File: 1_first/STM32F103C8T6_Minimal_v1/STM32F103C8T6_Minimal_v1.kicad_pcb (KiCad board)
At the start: 2 copper layers, 51.1 x 41.1 mm, 34 parts, among them J1 Conn_01x06, J2 USB_B_Micro, SW1 SW_SPDT, SW2 SW_Push, SW3 SW_Push, U1 AMS1117-3.3, U2 STM32F103C8Tx, U3 USBLC6-2SC6, Y1 8MHz

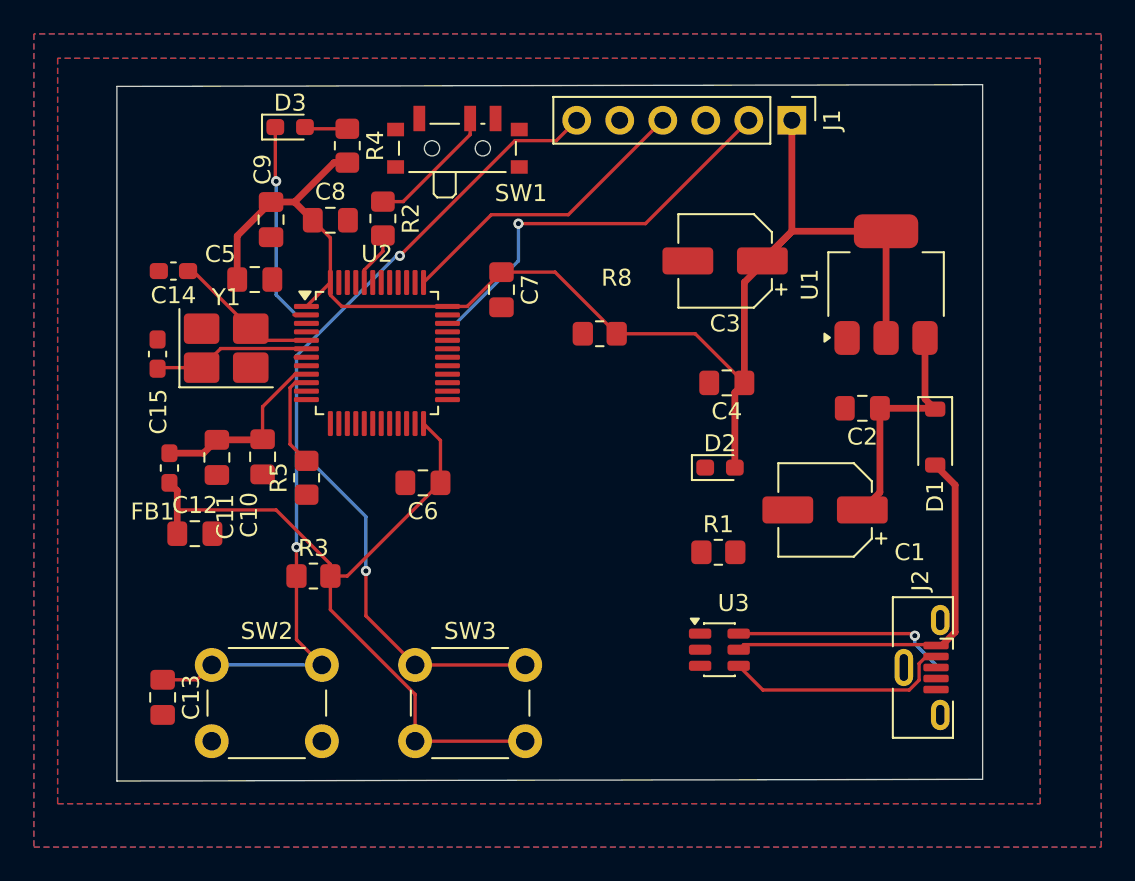
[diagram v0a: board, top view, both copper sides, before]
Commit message: fixed ground pad thermal issues
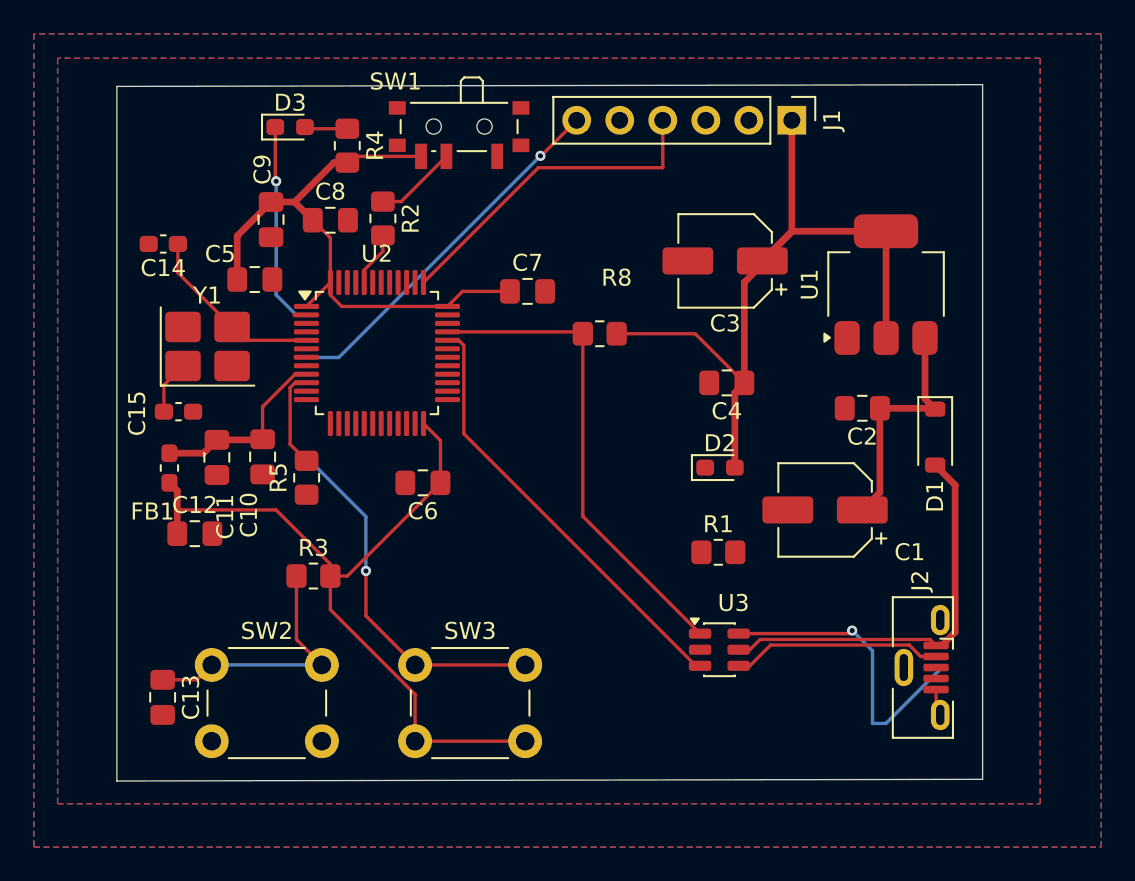
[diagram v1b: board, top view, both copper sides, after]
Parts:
- moved C15 3.62 mm to (108.5, 98.3), turned to 0 degrees
- moved C14 1.71 mm to (107.6, 88.4)
- moved C7 1.54 mm to (129.1, 91.2), turned to 0 degrees
- moved Y1 1.10 mm to (110.2, 94.5)
- moved SW1 0.63 mm to (125.1, 81.8), turned to 180 degrees
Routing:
- net PA12: track 0.00 -> 28.6 mm
- net PA11: track 0.00 -> 25.9 mm
- net /MCU/SWDIO: track 23.6 -> 0.00 mm, vias 1 -> 0
- net /MCU/NRST: track 51.6 -> 38.1 mm, vias 2 -> 1
- net /MCU/HSE_OUT: track 9.29 -> 3.17 mm
- net Net-(J2-D+): track 12.9 -> 18.1 mm
- net +3.3V: track 129.6 -> 125.2 mm
- net Net-(SW1-B): track 7.74 -> 4.86 mm
- net /MCU/HSE_IN: track 8.68 -> 10.9 mm
- net /MCU/SWCLK: track 18.1 -> 19.7 mm
- net Net-(J2-D-): track 13.6 -> 12.4 mm
- net GND: track 0.64 -> 1.60 mm

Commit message: DRC errors fixed
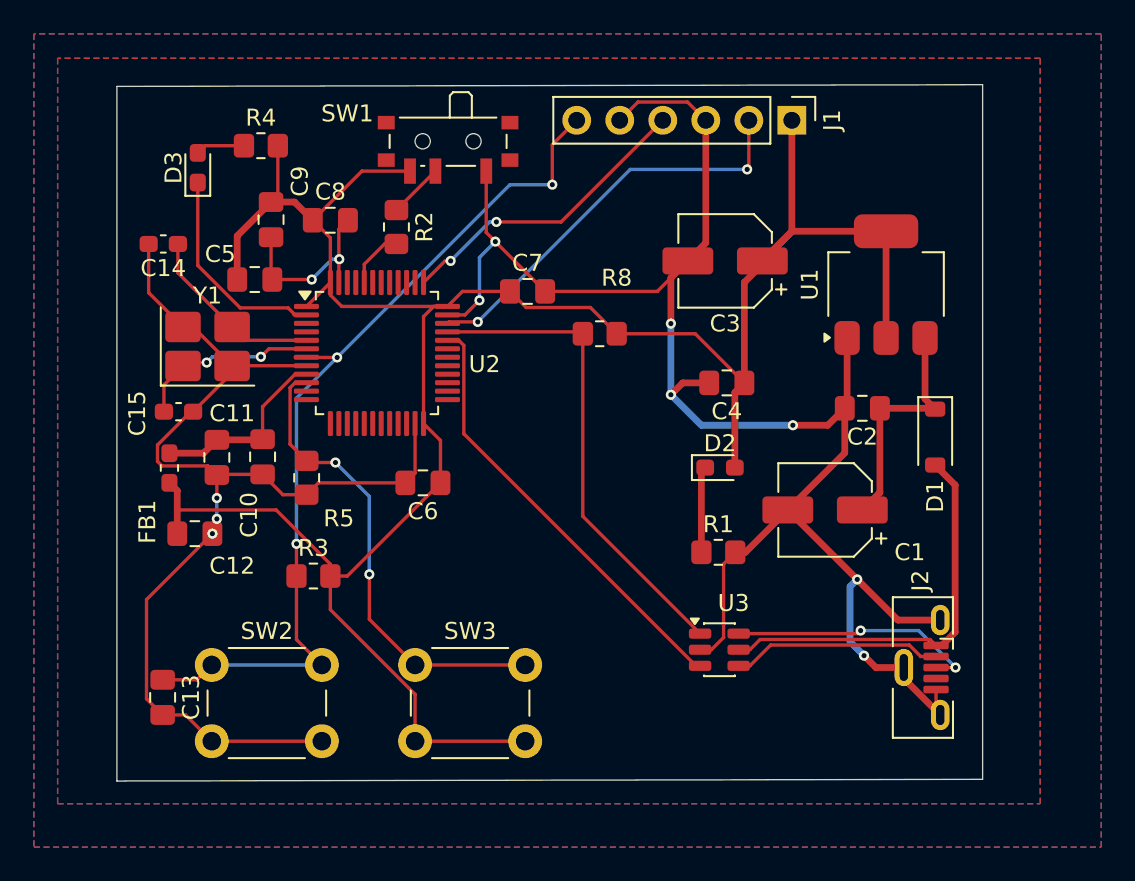
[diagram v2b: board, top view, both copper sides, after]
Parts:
- moved D3 5.96 mm to (109.7, 83.9), turned to 90 degrees
- moved R4 5.10 mm to (113.4, 82.6), turned to 0 degrees
- moved SW1 1.09 mm to (124.5, 82.7)
- moved R2 0.94 mm to (121.4, 87.4)
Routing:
- net GND: track 1.60 -> 185.0 mm, vias 0 -> 12
- net /MCU/SWDIO: track 0.00 -> 24.4 mm, vias 0 -> 2
- net +3.3V: track 125.2 -> 142.4 mm
- net /MCU/NRST: track 38.1 -> 53.3 mm, vias 1 -> 3
- net /MCU/HSE_OUT: track 3.17 -> 10.9 mm, vias 0 -> 2
- net Net-(D2-K): track 0.00 -> 5.09 mm
- net Net-(J2-D+): track 18.1 -> 14.9 mm, vias 1 -> 2
- net /MCU/SWCLK: track 19.7 -> 18.1 mm, vias 0 -> 2
- net Net-(SW1-B): track 4.86 -> 3.25 mm
- net Net-(U2-PA0): track 26.9 -> 27.9 mm, vias 1 -> 2
- net Net-(D3-K): track 12.4 -> 13.3 mm, vias 1 -> 0
